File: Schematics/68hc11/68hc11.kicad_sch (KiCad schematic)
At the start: 33 parts, among them J1 DB9_Female, J2 Screw_Terminal_01x10, J3 Screw_Terminal_01x10, J4 Screw_Terminal_01x10, J5 Screw_Terminal_01x10, SW1 Reset, U1 MC68HC11A1CC-PLLC, U10 MCP100-270D, U2 MC68B21, U3 74HC373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

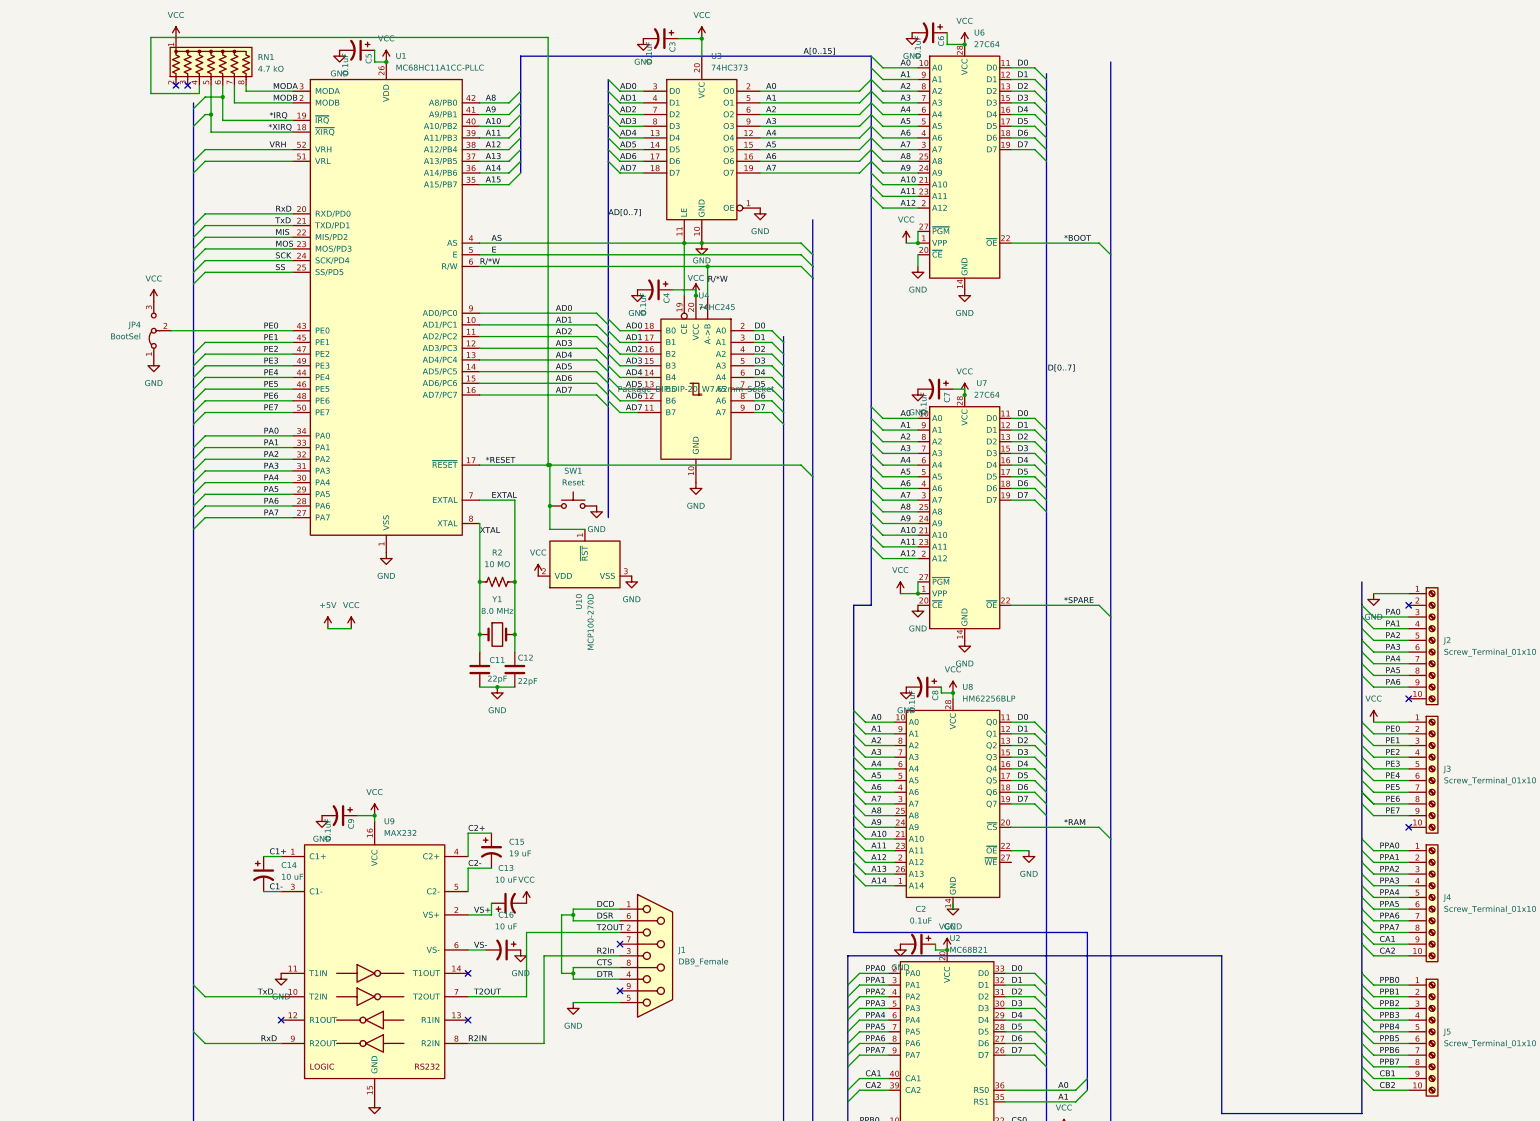
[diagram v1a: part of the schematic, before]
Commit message: Added power jack
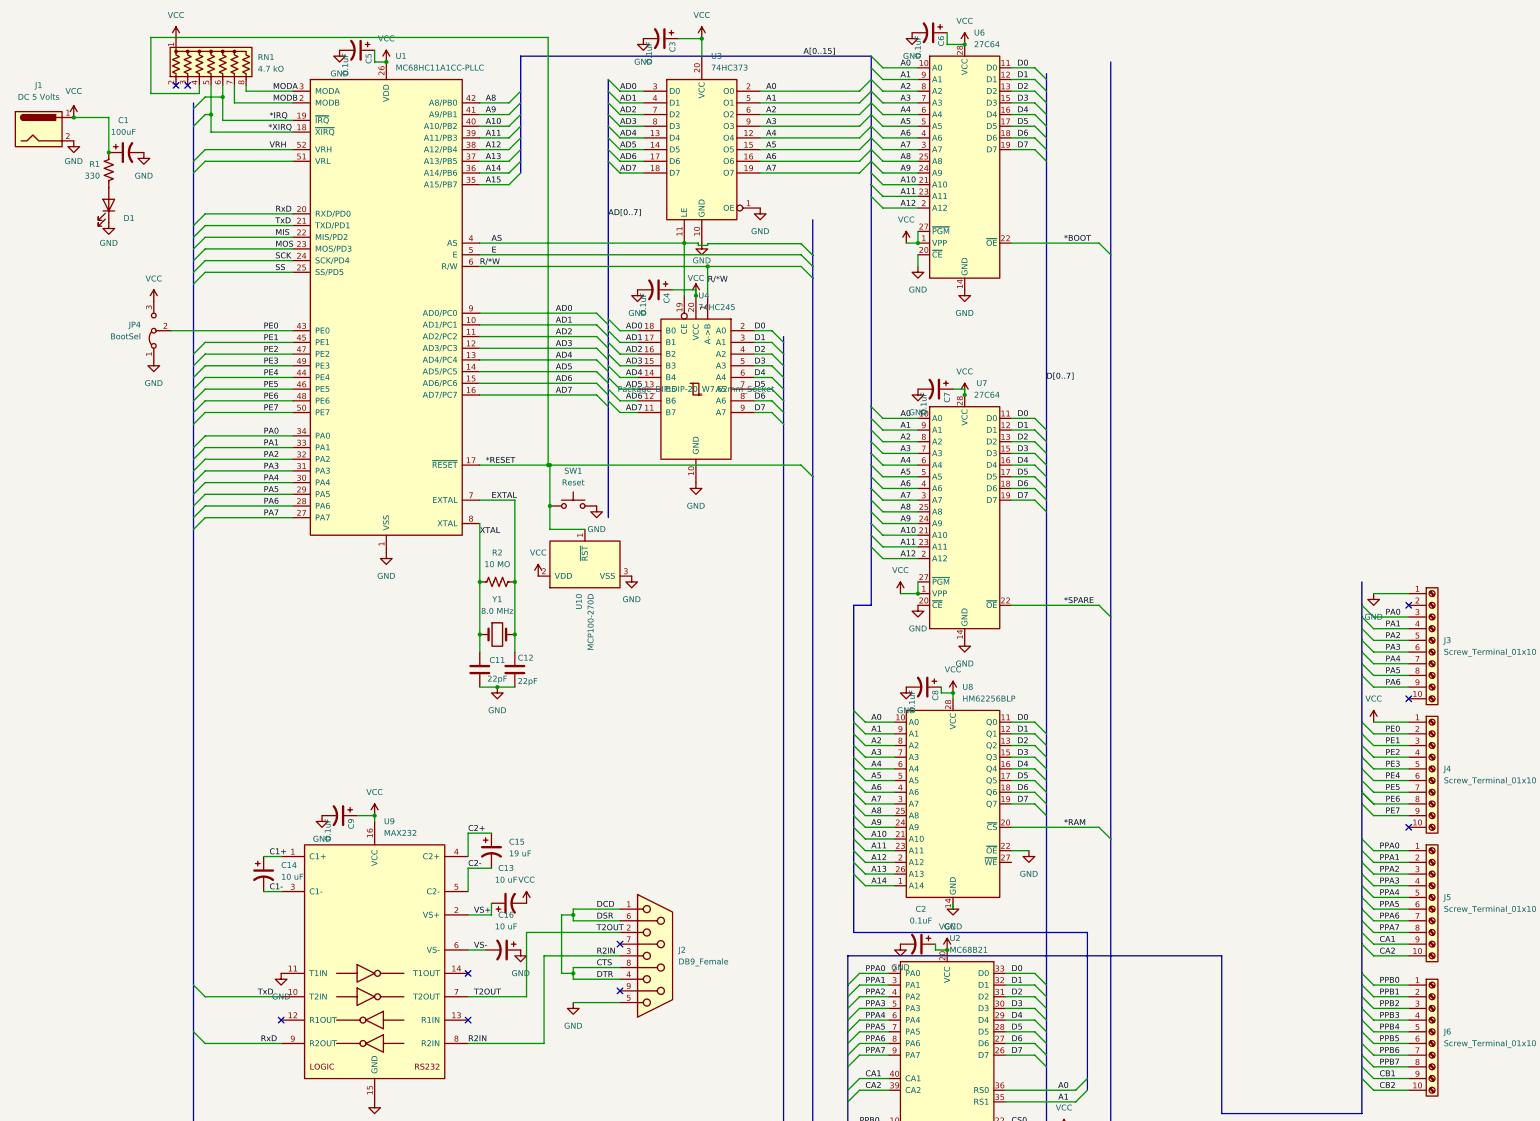
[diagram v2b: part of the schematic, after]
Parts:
- added C1: 100uF, Capacitor_THT:CP_Radial_D5.0mm_P2.00mm, symbol Device:C_Polarized_US
- added D1: LED, LED_THT:LED_D5.0mm, symbol Device:LED
- added J1: DC 5 Volts, Connector_BarrelJack:BarrelJack_CUI_PJ-063AH_Horizontal_CircularHoles, symbol Connector:Jack-DC
- added R1: 330, Resistor_THT:R_Axial_DIN0204_L3.6mm_D1.6mm_P7.62mm_Horizontal, symbol Device:R_US
- renumbered J1 to J2, J2 to J3, J3 to J4, J4 to J5, J5 to J6
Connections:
- net GND: now also C1.2, D1.1 (K), J1.2; no longer U1.4 (AS), U3.11 (LE), U4.19 (CE)
- net +5V renamed VCC
- net VCC: now also C1.1, J1.1, R1.2
- new net: D1.2 (A), R1.1
- new net AS: U1.4 (AS), U3.11 (LE), U4.19 (CE)

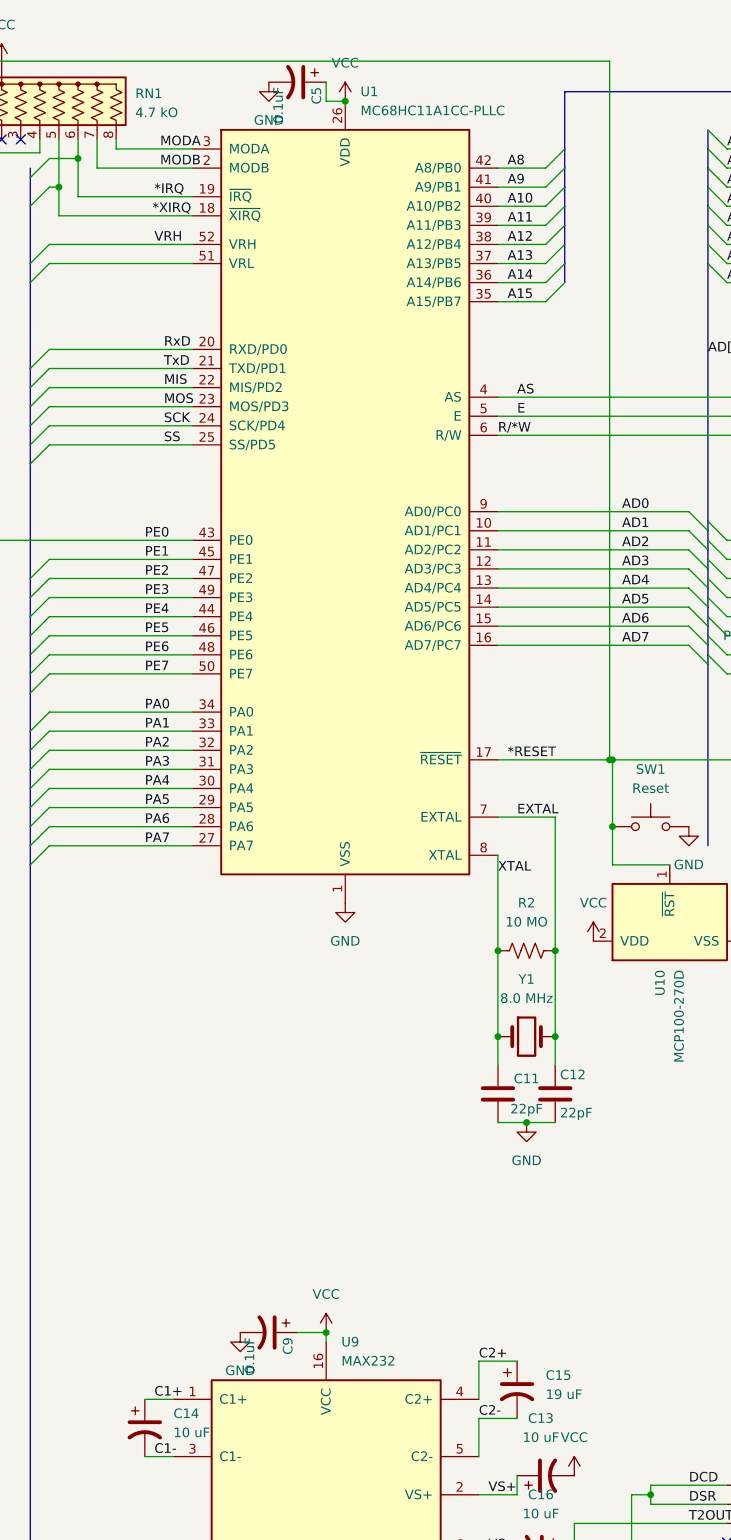
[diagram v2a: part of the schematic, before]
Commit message: Updated bad component values
Also generated first Bill Of Materials
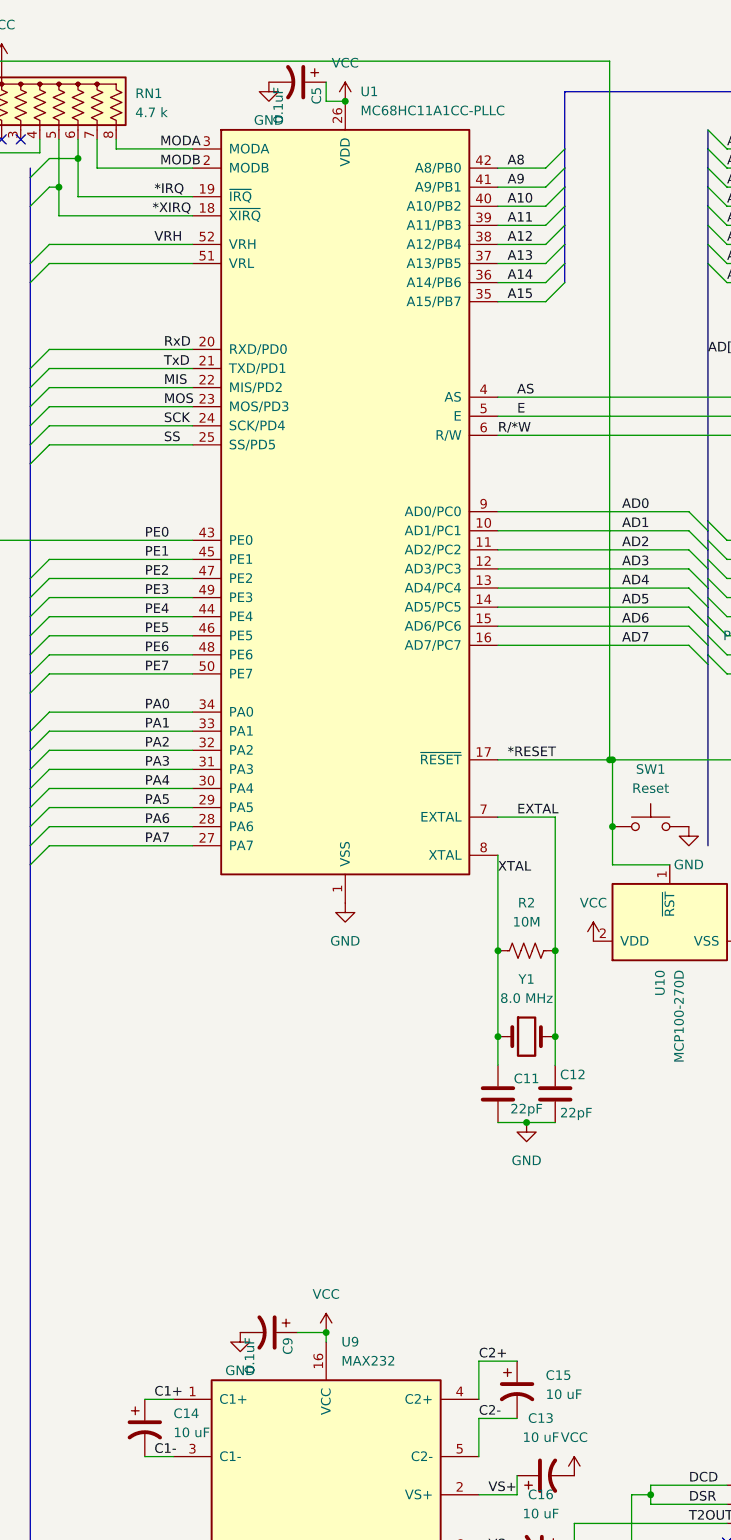
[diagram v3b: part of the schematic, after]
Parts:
- C15: value 19 uF -> 10 uF
- R2: value 10 MO -> 10M
- RN1: value 4.7 kO -> 4.7 k
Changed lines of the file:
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@@
       (effects (font (size 1.27 1.27)) (justify left))
     )
-    (property "Value" "19 uF" (id 1) (at 125.73 192.4049 0)
+    (property "Value" "10 uF" (id 1) (at 125.73 192.4049 0)
       (effects (font (size 1.27 1.27)) (justify left))
     )
@@
       (effects (font (size 1.27 1.27)) (justify left))
     )
-    (property "Value" "4.7 kO" (id 1) (at 71.12 21.8439 0)
+    (property "Value" "4.7 k" (id 1) (at 71.12 21.8439 0)
       (effects (font (size 1.27 1.27)) (justify left))
     )
@@
     (in_bom yes) (on_board yes) (fields_autoplaced)
     (property "Reference" "R2" (id 0) (at 123.19 127 90))
-    (property "Value" "10 MO" (id 1) (at 123.19 129.54 90))
+    (property "Value" "10M" (id 1) (at 123.19 129.54 90))
     (property "Footprint" "Resistor_THT:R_Axial_DIN0309_L9.0mm_D3.2mm_P12.70mm_Horizontal" (id 2) (at 122.936 134.366 90)
       (effects (font (size 1.27 1.27)) hide)
@@
     )
     (path "/058e48dd-abfb-4356-a3ec-3f1c1d300d65"
-      (reference "C15") (unit 1) (value "19 uF") (footprint "Capacitor_THT:CP_Radial_D5.0mm_P2.00mm")
+      (reference "C15") (unit 1) (value "10 uF") (footprint "Capacitor_THT:CP_Radial_D5.0mm_P2.00mm")
     )
     (path "/d5278e62-1e47-4c52-b959-29dd41e34108"
@@
     )
     (path "/d271d8e0-6f73-4dff-889e-b4e6826a44bf"
-      (reference "R2") (unit 1) (value "10 MO") (footprint "Resistor_THT:R_Axial_DIN0309_L9.0mm_D3.2mm_P12.70mm_Horizontal")
+      (reference "R2") (unit 1) (value "10M") (footprint "Resistor_THT:R_Axial_DIN0309_L9.0mm_D3.2mm_P12.70mm_Horizontal")
     )
     (path "/0ecf9e04-6c55-4a4d-b4e8-8b3c906e6141"
-      (reference "RN1") (unit 1) (value "4.7 kO") (footprint "Resistor_THT:R_Array_SIP8")
+      (reference "RN1") (unit 1) (value "4.7 k") (footprint "Resistor_THT:R_Array_SIP8")
     )
     (path "/a8990ba7-c40c-4a12-abcb-6187090269d2"

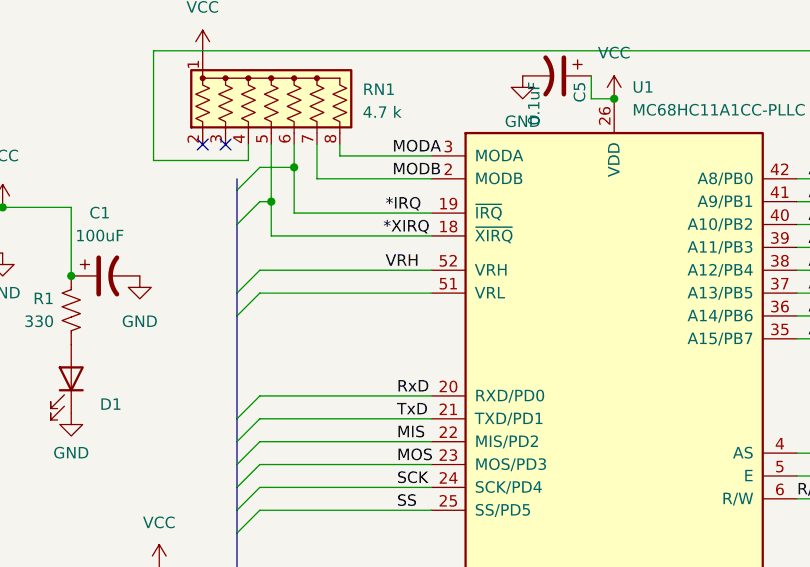
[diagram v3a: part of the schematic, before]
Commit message: Continueing to rework traces
Addec VCC Plane
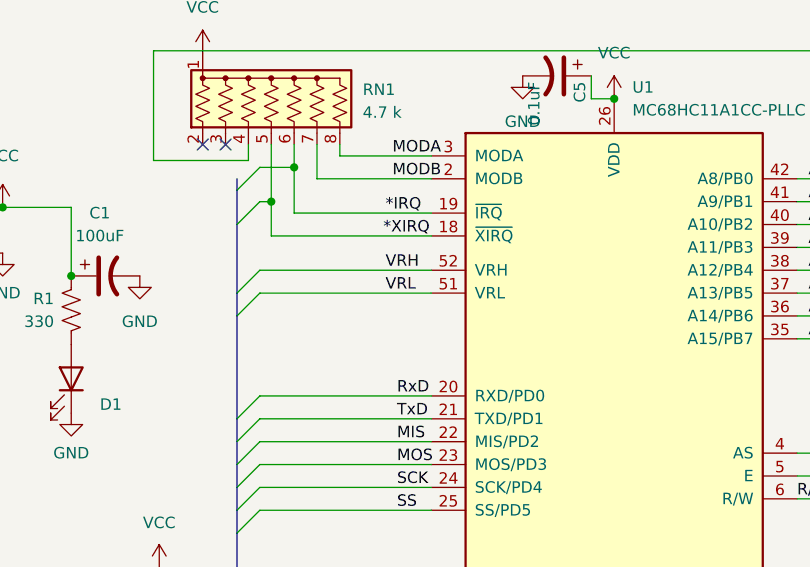
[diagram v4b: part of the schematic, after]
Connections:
- net VRL: now reaches U1.51 (VRL)
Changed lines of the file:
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@@
+    (effects (font (size 1.27 1.27)) (justify left bottom))
+  )
+  (label "VRL" (at 73.66 41.91 0)
     (effects (font (size 1.27 1.27)) (justify left bottom))
   )
